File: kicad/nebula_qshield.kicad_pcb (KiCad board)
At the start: 4 copper layers, 150 x 120 mm, 164 parts, among them J1 J1, J10 J10, J11 J11, J12 J12, J13 J13, J14 J14, J15 J15, J16 J16, J17 J17, J18 J18, J19 J19, J2 J2, J20 J20, J21 Arduino UNO Q Shield, J3 J3, J4 J4, J5 J5, J6 J6, J7 J7, J8 J8, J9 J9, K1 HF46F-12-HS1, K2 HF46F-12-HS1, Q1 IRLZ44NPBF, Q2 IRLZ44NPBF, Q3 2N7002, Q4 2N7002, Q5 IRLZ44NPBF, SW1 RESET, T1 Transformer_SP_2S, T2 Transformer_SP_2S, T3 Transformer_SP_2S, U1 TPS54302DDCR, U10 MCP6002, U11 MCP6002, U12 SN6501, U13 AMC1301, U14 HX711, U15 MAX485ESA, U16 PC817X2NIP, U17 IR2104SPBF, U18 PC817X1NIP, U19 PC817X1NIP, U2 AMS1117-3.3, U20 MCP6002, U21 ISO1541, U22 SC16IS740, U23 SN74LVC1G04, U3 TPS3823-33DBVR, U4 MCP6002, U5 SN6501, U6 AMC1301, U7 MCP6002, U8 SN6501, U9 AMC1301, Y1 1.8432MHz

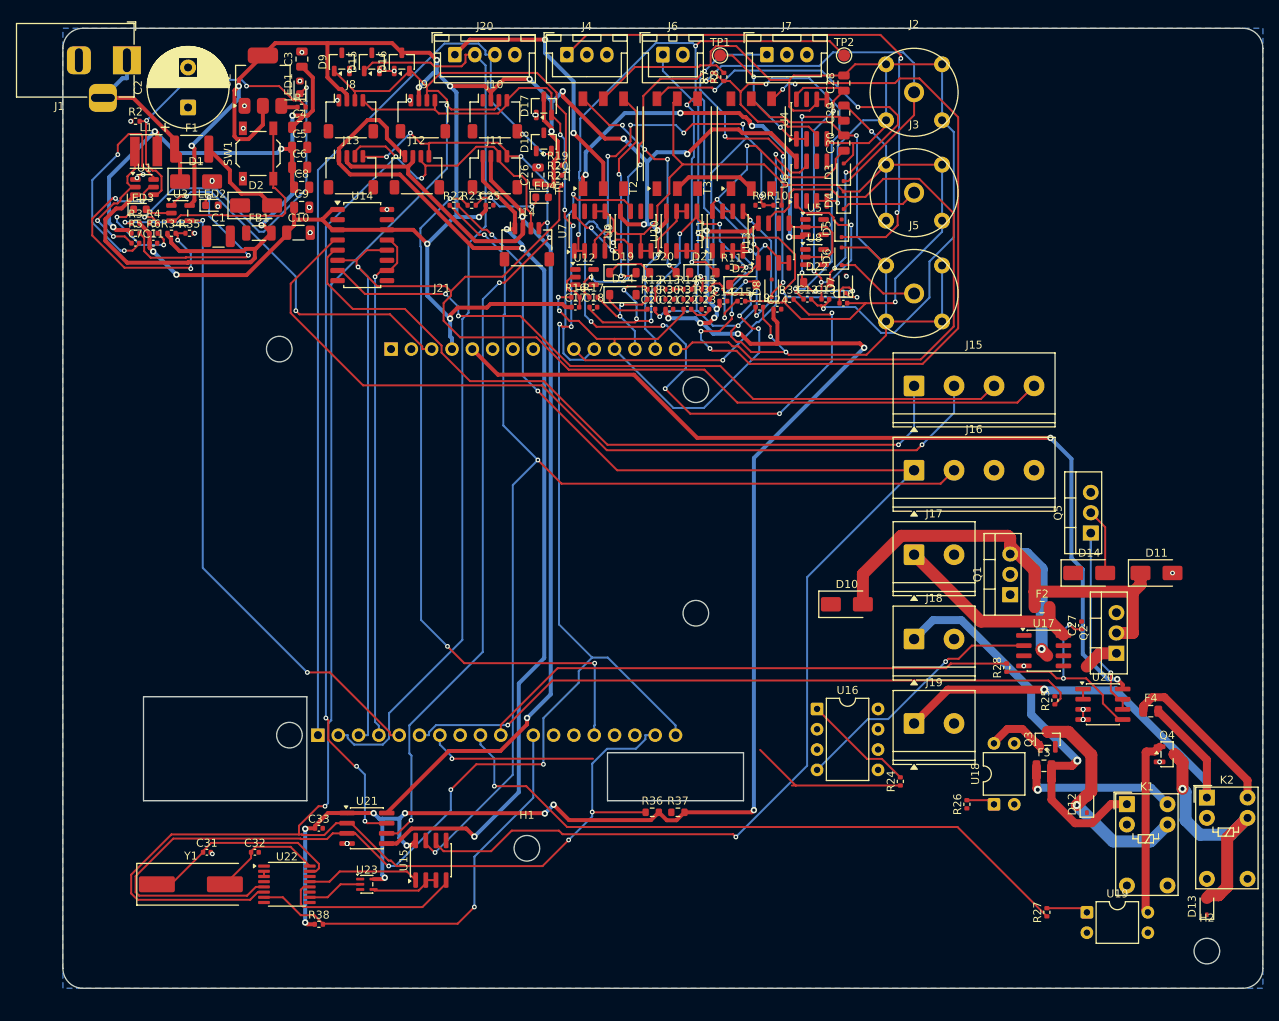
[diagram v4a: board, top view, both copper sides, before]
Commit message: feat(pcb): ruteo manual GND y stubs — DRC 0, 72 unconnected, vía 0.5/0.2, fix PUMP_DIR
Co-Authored-By: Devin AI <158243242+devin-ai-integration[bot]@users.noreply.github.com>
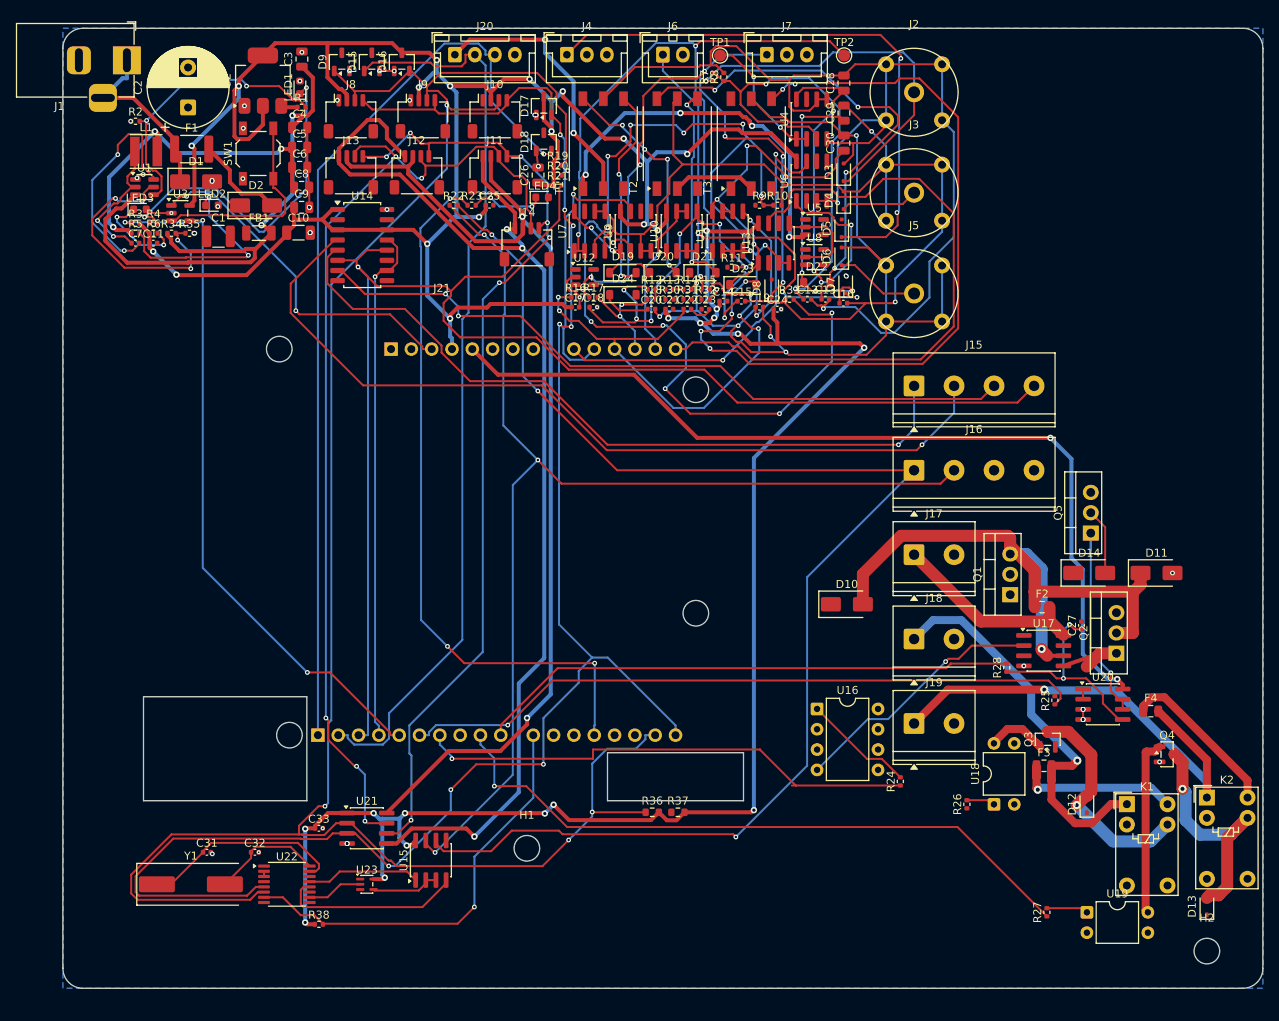
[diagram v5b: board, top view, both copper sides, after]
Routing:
- net /PUMP_DIR: track 41.1 -> 63.2 mm
- net GND: track 32.6 -> 44.5 mm, vias 36 -> 50
- net /Actuator Drivers/MOTOR_LO: track 4.40 -> 9.24 mm
- net /Actuator Drivers/MOTOR_VS: track 74.5 -> 76.6 mm
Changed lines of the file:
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@@
 	)
 	(segment
+		(start 22.8 17.88)
+		(end 22.55 15.38)
+		(width 0.25)
+		(layer "F.Cu")
+		(net "GND")
+	)
+	(segment
 		(start 68.715 25.825)
 		(end 69.985 25.825)
@@
 	)
 	(segment
+		(start 22.8 17.88)
+		(end 22.8 20.38)
+		(width 0.25)
+		(layer "F.Cu")
+		(net "GND")
+	)
+	(segment
 		(start 72.79 33.3334)
 		(end 72.2762 33.8472)
@@
 	)
 	(segment
+		(start 22.55 12.88)
+		(end 22.55 10.38)
+		(width 0.25)
+		(layer "F.Cu")
+		(net "GND")
+	)
+	(segment
+		(start 22.55 12.88)
+		(end 22.55 15.38)
+		(width 0.25)
+		(layer "F.Cu")
+		(net "GND")
+	)
+	(segment
 		(start 55.379 30.8438)
 		(end 55.9268 30.8438)
@@
 	)
 	(segment
+		(start 51.4 15.24)
+		(end 51.17 13.3375)
+		(width 0.25)
+		(layer "F.Cu")
+		(net "GND")
+	)
+	(segment
 		(start 71.2772 33.8472)
 		(end 70.54 33.11)
@@
 	)
 	(via
+		(at 51.4 15.24)
+		(size 0.5)
+		(drill 0.2)
+		(layers "F.Cu" "B.Cu")
+		(net "GND")
+	)
+	(via
+		(at 24.48 98)
+		(size 0.5)
+		(drill 0.2)
+		(layers "F.Cu" "B.Cu")
+		(net "GND")
+	)
+	(via
 		(at 10.65 17.15)
 		(size 0.6)
@@
 	)
 	(via
+		(at 119.525 83.135)
+		(size 0.5)
+		(drill 0.2)
+		(layers "F.Cu" "B.Cu")
+		(net "GND")
+	)
+	(via
+		(at 56.59 31.62)
+		(size 0.5)
+		(drill 0.2)
+		(layers "F.Cu" "B.Cu")
+		(net "GND")
+	)
+	(via
+		(at 22.8 20.38)
+		(size 0.5)
+		(drill 0.2)
+		(layers "F.Cu" "B.Cu")
+		(net "GND")
+	)
+	(via
+		(at 58.79 32.86)
+		(size 0.5)
+		(drill 0.2)
+		(layers "F.Cu" "B.Cu")
+		(net "GND")
+	)
+	(via
+		(at 119.525 84.405)
+		(size 0.5)
+		(drill 0.2)
+		(layers "F.Cu" "B.Cu")
+		(net "GND")
+	)
+	(via
+		(at 81.79 33.11)
+		(size 0.5)
+		(drill 0.2)
+		(layers "F.Cu" "B.Cu")
+		(net "GND")
+	)
+	(via
 		(at 22.875 23.55)
 		(size 0.6)
@@
 	)
 	(via
+		(at 22.925 23.55)
+		(size 0.5)
+		(drill 0.2)
+		(layers "F.Cu" "B.Cu")
+		(net "GND")
+	)
+	(via
 		(at 35.35 7)
 		(size 0.6)
@@
 	)
 	(via
+		(at 16.48 101)
+		(size 0.5)
+		(drill 0.2)
+		(layers "F.Cu" "B.Cu")
+		(net "GND")
+	)
+	(via
 		(at 1.2625 16.7)
 		(size 0.6)
@@
 	)
 	(via
+		(at 27.525 99.905)
+		(size 0.5)
+		(drill 0.2)
+		(layers "F.Cu" "B.Cu")
+		(net "GND")
+	)
+	(via
 		(at 0.47 9.62)
 		(size 0.6)
@@
 	)
 	(via
+		(at 8.34 23.62)
+		(size 0.5)
+		(drill 0.2)
+		(layers "F.Cu" "B.Cu")
+		(net "GND")
+	)
+	(via
 		(at 10.68 101.2)
 		(size 0.6)
@@
 	)
 	(via
+		(at 5.5625 21.1)
+		(size 0.5)
+		(drill 0.2)
+		(layers "F.Cu" "B.Cu")
+		(net "GND")
+	)
+	(via
 		(at 10.65 17)
 		(size 0.6)
@@
 	)
 	(via
+		(at 89.85 28.9)
+		(size 0.5)
+		(drill 0.2)
+		(layers "F.Cu" "B.Cu")
+		(net "GND")
+	)
+	(via
 		(at 89.95 29)
 		(size 0.6)
@@
 	)
 	(segment
+		(start 115.05 76.4359)
+		(end 117.0714 76.4359)
+		(width 0.5)
+		(layer "F.Cu")
+		(net "/Actuator Drivers/MOTOR_VS")
+	)
+	(segment
 		(start 92 70)
 		(end 92 66.2224)
@@
 		(net "/PUMP_DIR")
 	)
+	(segment
+		(start 79.1525 88.15)
+		(end 79.1525 88.1987)
+		(width 0.25)
+		(layer "F.Cu")
+		(net "/PUMP_DIR")
+	)
+	(segment
+		(start 58.2681 89.3054)
+		(end 58.2681 88.15)
+		(width 0.25)
+		(layer "F.Cu")
+		(net "/PUMP_DIR")
+	)
+	(segment
+		(start 58.2681 88.15)
+		(end 79.1525 88.15)
+		(width 0.25)
+		(layer "F.Cu")
+		(net "/PUMP_DIR")
+	)
 	(via
 		(at 40.6342 89.3054)
@@
 		(layer "F.Cu")
 		(net "/Actuator Drivers/MOTOR_LO")
+	)
+	(segment
+		(start 117.0714 77.7059)
+		(end 121.642 76.1281)
+		(width 0.5)
+		(layer "F.Cu")
+		(net "/Actuator Drivers/MOTOR_LO")

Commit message: feat(pcb): Fase 6 inicio — relaja vías Power/HighCurrent a 0.5/0.2 mm y cierra 2 nets de potencia, DRC 0, 70 unconnected
Co-Authored-By: Devin AI <158243242+devin-ai-integration[bot]@users.noreply.github.com>
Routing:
- net /12V_RAIL: track 0.14 -> 2.68 mm, vias 0 -> 2
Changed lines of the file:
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@@
+		(net "/12V_RAIL")
+	)
+	(via
+		(at 112.1214 73.8959)
+		(size 0.5)
+		(drill 0.2)
+		(layers "F.Cu" "B.Cu")
+		(net "/12V_RAIL")
+	)
+	(via
+		(at 112.1214 76.4359)
+		(size 0.5)
+		(drill 0.2)
+		(layers "F.Cu" "B.Cu")
+		(net "/12V_RAIL")
+	)
+	(segment
+		(start 112.1214 73.8959)
+		(end 112.1214 76.4359)
+		(width 0.5)
+		(layer "B.Cu")
 		(net "/12V_RAIL")
 	)
